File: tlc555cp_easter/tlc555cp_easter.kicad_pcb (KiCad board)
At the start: 2 copper layers, 68.6 x 78.7 mm, 19 parts, among them SW1 SW_MEC_5E, U1 TLC555xP

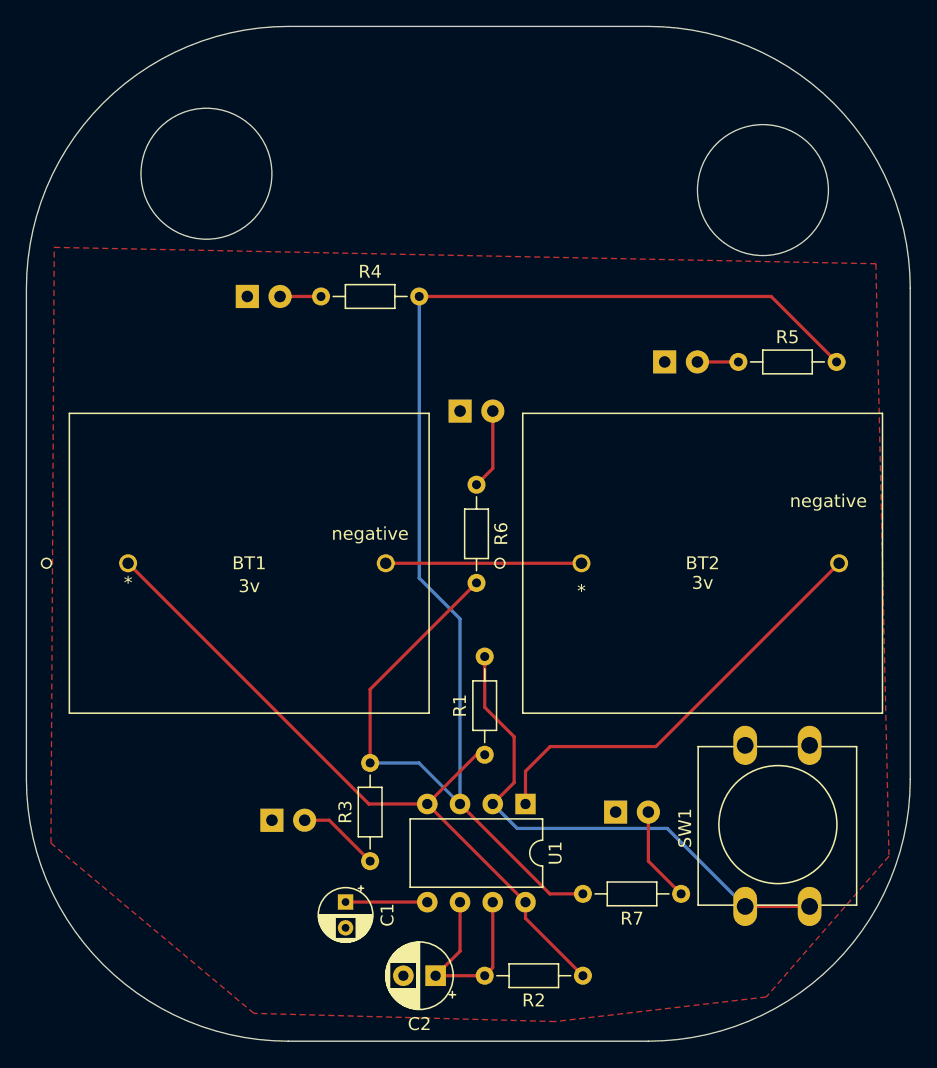
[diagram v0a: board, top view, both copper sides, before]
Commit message: Fix switch footprint pad assignment.
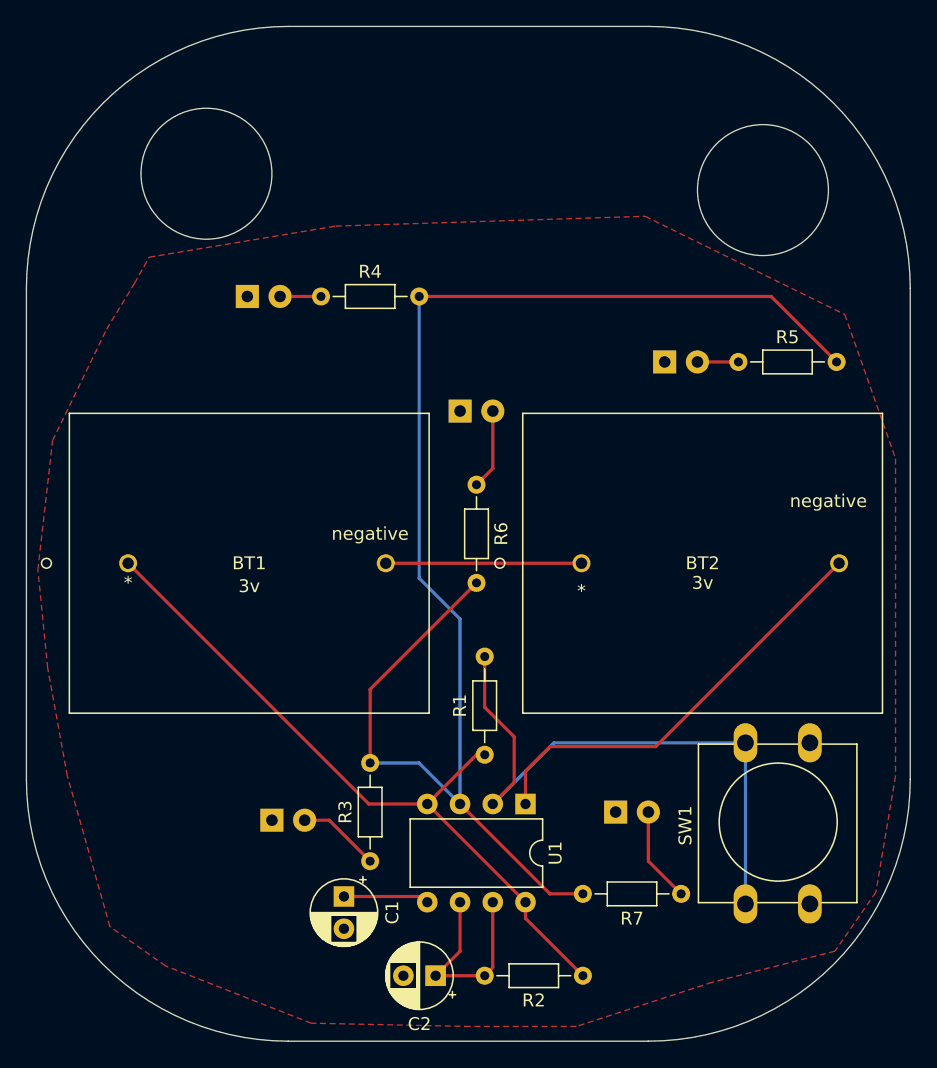
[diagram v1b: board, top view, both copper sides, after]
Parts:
- C1: value 0.1u -> 0.1U; footprint Capacitor_THT:CP_Radial_D4.0mm_P2.00mm -> Capacitor_THT:CP_Radial_D5.0mm_P2.50mm
- moved C1 0.45 mm to (199.9, 133.6)
- moved SW1 0.20 mm to (231.1, 134.1)
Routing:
- net Net-(R1-Pad2): track 41.0 -> 47.1 mm
